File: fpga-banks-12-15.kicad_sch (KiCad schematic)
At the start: 17 parts, among them U15 XC7K160T-FFG676

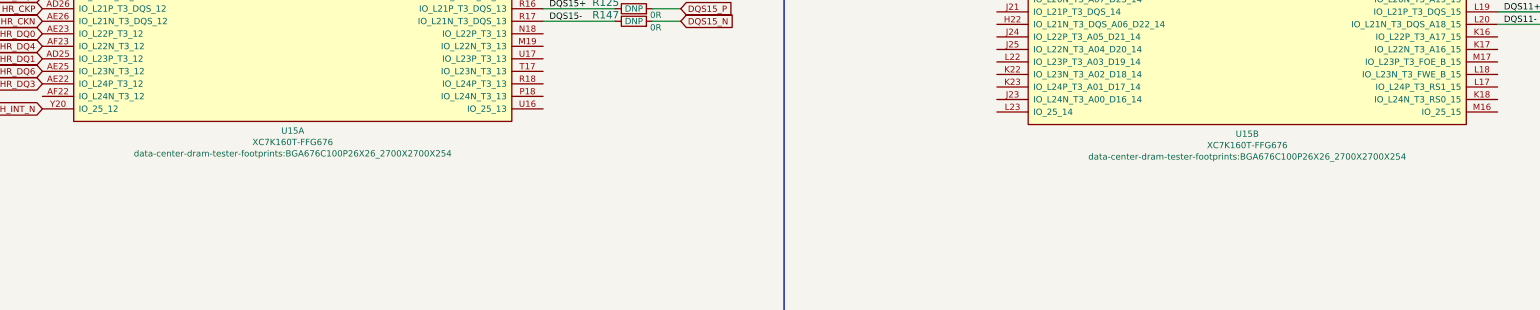
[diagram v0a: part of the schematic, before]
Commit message: Update FPGA symbol (die to pad length), initial fanout for die [1..4]
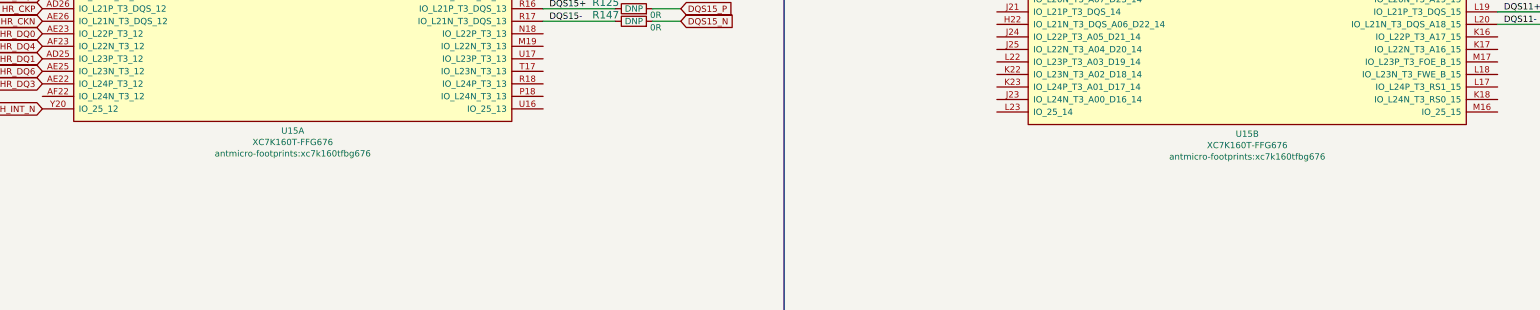
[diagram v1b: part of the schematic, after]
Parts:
- U15: footprint data-center-dram-tester-footprints:BGA676C100P26X26_2700X2700X254 -> antmicro-footprints:xc7k160tfbg676
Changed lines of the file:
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@@
     (property "Reference" "U15" (id 0) (at 110.49 220.98 0))
     (property "Value" "XC7K160T-FFG676" (id 1) (at 110.49 223.2914 0))
-    (property "Footprint" "data-center-dram-tester-footprints:BGA676C100P26X26_2700X2700X254" (id 2) (at 110.49 225.6028 0))
+    (property "Footprint" "antmicro-footprints:xc7k160tfbg676" (id 2) (at 110.49 225.6028 0))
     (property "Datasheet" "" (id 3) (at 110.49 145.415 0))
     (pin "AA21")
@@
     (property "Reference" "U15" (id 0) (at 304.165 221.615 0))
     (property "Value" "XC7K160T-FFG676" (id 1) (at 304.165 223.9264 0))
-    (property "Footprint" "data-center-dram-tester-footprints:BGA676C100P26X26_2700X2700X254" (id 2) (at 304.165 226.2378 0))
+    (property "Footprint" "antmicro-footprints:xc7k160tfbg676" (id 2) (at 304.165 226.2378 0))
     (property "Datasheet" "" (id 3) (at 304.165 146.05 0))
     (pin "AA21")

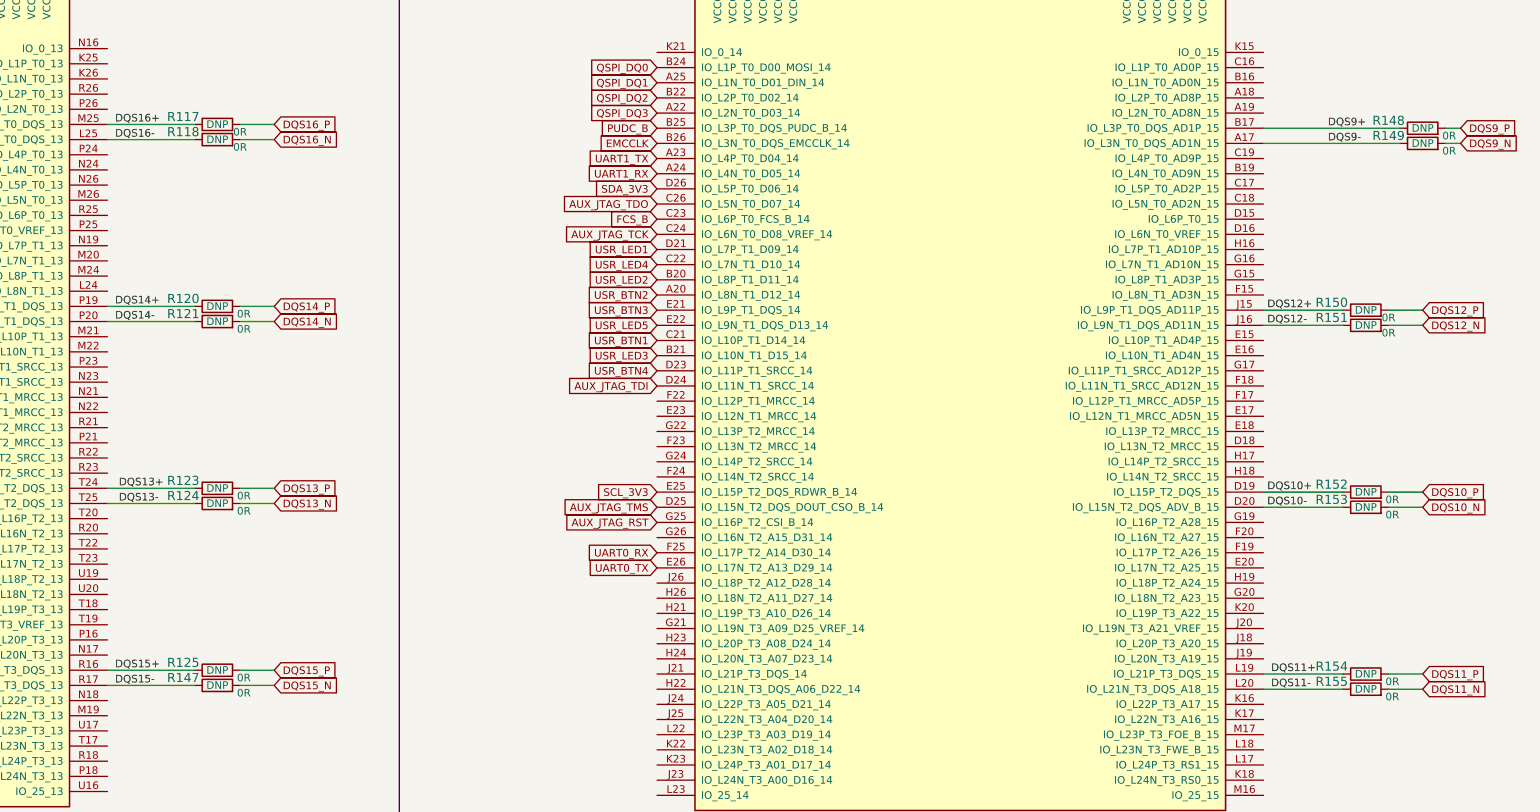
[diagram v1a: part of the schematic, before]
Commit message: Add new pinout for bank 32 and 34, create custom DRC rules for DDR, initial routing for die 6,7,9
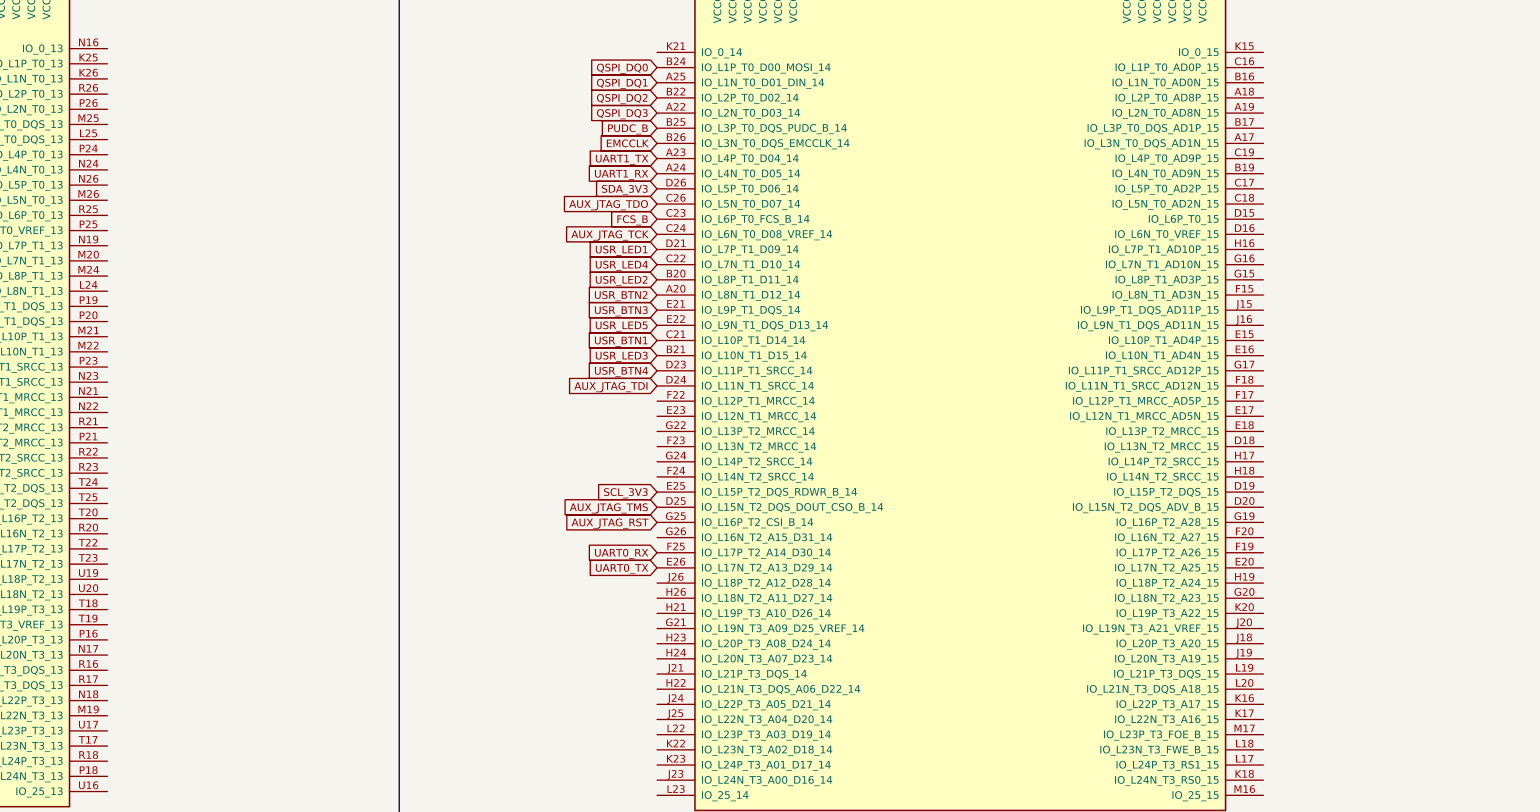
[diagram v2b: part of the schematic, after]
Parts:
- removed R117, R118, R120, R121, R123, R124, R125, R147, R148, R149, R150, R151, R152, R153, R154, R155: R_0R_0201, data-center-dram-tester-footprints:0201-res, symbol data-center-dram-tester:R_0R_0201
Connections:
- net DQS10+: no longer names the net of U15.D19 (IO_L15P_T2_DQS_15)
- net DQS10-: no longer names the net of U15.D20 (IO_L15N_T2_DQS_ADV_B_15)
- net DQS11+: no longer names the net of U15.L19 (IO_L21P_T3_DQS_15)
- net DQS11-: no longer names the net of U15.L20 (IO_L21N_T3_DQS_A18_15)
- net DQS12+: no longer names the net of U15.J15 (IO_L9P_T1_DQS_AD11P_15)
- net DQS12-: no longer names the net of U15.J16 (IO_L9N_T1_DQS_AD11N_15)
- net DQS13+: no longer names the net of U15.T24 (IO_L15P_T2_DQS_13)
- net DQS13-: no longer names the net of U15.T25 (IO_L15N_T2_DQS_13)
- net DQS14+: no longer names the net of U15.P19 (IO_L9P_T1_DQS_13)
- net DQS14-: no longer names the net of U15.P20 (IO_L9N_T1_DQS_13)
- net DQS15+: no longer names the net of U15.R16 (IO_L21P_T3_DQS_13)
- net DQS15-: no longer names the net of U15.R17 (IO_L21N_T3_DQS_13)
- net DQS16+: no longer names the net of U15.M25 (IO_L3P_T0_DQS_13)
- net DQS16-: no longer names the net of U15.L25 (IO_L3N_T0_DQS_13)
- net DQS9+: no longer names the net of U15.B17 (IO_L3P_T0_DQS_AD1P_15)
- net DQS9-: no longer names the net of U15.A17 (IO_L3N_T0_DQS_AD1N_15)

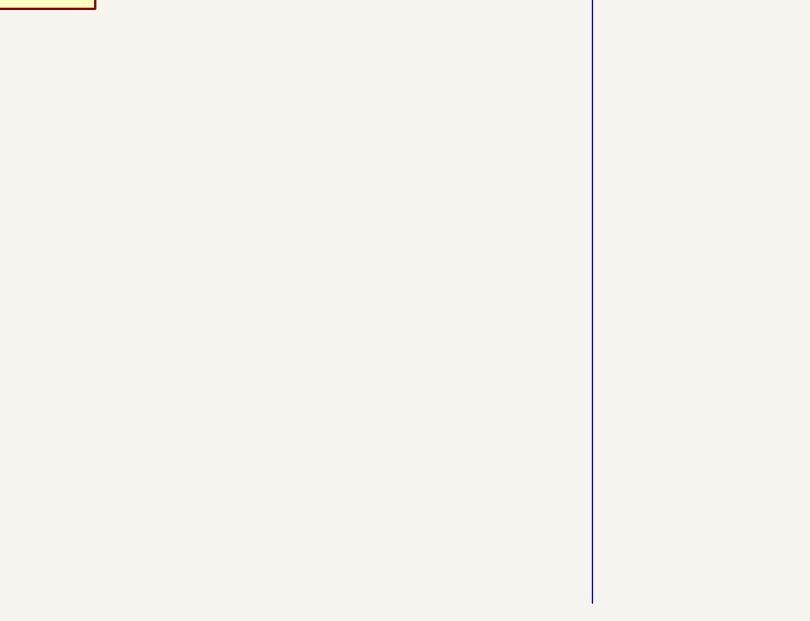
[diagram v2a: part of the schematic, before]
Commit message: Finish assigning address, command and control pins. Finish initial rerouting of DDR4 interface
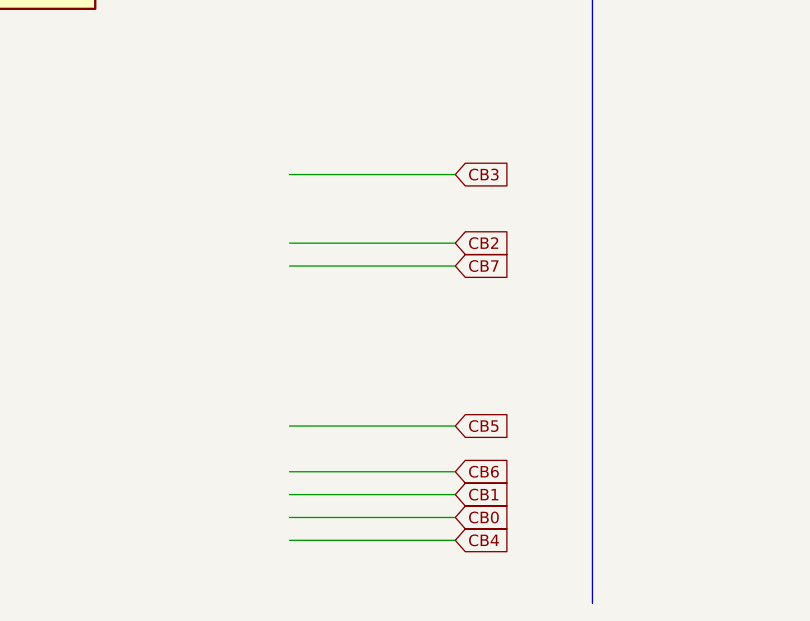
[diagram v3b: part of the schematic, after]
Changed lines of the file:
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@@
+    (stroke (width 0) (type default) (color 0 0 0 0))
+  )
+  (wire (pts (xy 176.53 278.13) (xy 194.945 278.13))
     (stroke (width 0) (type default) (color 0 0 0 0))
   )
@@
     (stroke (width 0) (type default) (color 0 0 0 0))
   )
+  (wire (pts (xy 176.53 270.51) (xy 194.945 270.51))
+    (stroke (width 0) (type default) (color 0 0 0 0))
+  )
   (wire (pts (xy 140.97 66.04) (xy 143.51 66.04))
     (stroke (width 0) (type default) (color 0 0 0 0))
@@
     (stroke (width 0) (type default) (color 0 0 0 0))
   )
+  (wire (pts (xy 176.53 275.59) (xy 194.945 275.59))
+    (stroke (width 0) (type default) (color 0 0 0 0))
+  )
   (wire (pts (xy 74.93 71.755) (xy 74.93 66.04))
     (stroke (width 0) (type default) (color 0 0 0 0))
@@
     (stroke (width 0) (type default) (color 0 0 0 0))
   )
+  (wire (pts (xy 176.53 265.43) (xy 194.945 265.43))
+    (stroke (width 0) (type default) (color 0 0 0 0))
+  )
   (wire (pts (xy 151.13 71.755) (xy 151.13 66.04))
     (stroke (width 0) (type default) (color 0 0 0 0))
@@
     (stroke (width 0) (type default) (color 0 0 0 0))
   )
+  (wire (pts (xy 176.53 247.65) (xy 194.945 247.65))
+    (stroke (width 0) (type default) (color 0 0 0 0))
+  )
   (wire (pts (xy 88.9 66.04) (xy 88.9 62.23))
     (stroke (width 0) (type default) (color 0 0 0 0))
@@
     (stroke (width 0) (type default) (color 0 0 0 0))
   )
+  (wire (pts (xy 176.53 237.49) (xy 194.945 237.49))
+    (stroke (width 0) (type default) (color 0 0 0 0))
+  )
   (wire (pts (xy 72.39 66.04) (xy 74.93 66.04))
     (stroke (width 0) (type default) (color 0 0 0 0))
@@
     (stroke (width 0) (type default) (color 0 0 0 0))
   )
+  (wire (pts (xy 176.53 245.11) (xy 194.945 245.11))
+    (stroke (width 0) (type default) (color 0 0 0 0))
+  )
   (wire (pts (xy 266.065 72.39) (xy 266.065 66.675))
+    (stroke (width 0) (type default) (color 0 0 0 0))
+  )
+  (wire (pts (xy 176.53 273.05) (xy 194.945 273.05))
     (stroke (width 0) (type default) (color 0 0 0 0))
   )
@@
     )
   )
+  (global_label "CB6" (shape input) (at 194.945 270.51 0) (fields_autoplaced)
+    (effects (font (size 1.27 1.27)) (justify left))
+    (property "Intersheet References" "${INTERSHEET_REFS}" (id 0) (at -177.165 76.835 0)
+      (effects (font (size 1.27 1.27)) hide)
+    )
+  )
   (global_label "HR_CKP" (shape input) (at 59.69 196.215 180) (fields_autoplaced)
     (effects (font (size 1.27 1.27)) (justify right))
@@
     )
   )
+  (global_label "CB5" (shape input) (at 194.945 265.43 0) (fields_autoplaced)
+    (effects (font (size 1.27 1.27)) (justify left))
+    (property "Intersheet References" "${INTERSHEET_REFS}" (id 0) (at -177.165 76.835 0)
+      (effects (font (size 1.27 1.27)) hide)
+    )
+  )
   (global_label "HR_DQ6" (shape input) (at 59.69 208.915 180) (fields_autoplaced)
     (effects (font (size 1.27 1.27)) (justify right))
@@
     )
   )
+  (global_label "CB0" (shape input) (at 194.945 275.59 0) (fields_autoplaced)
+    (effects (font (size 1.27 1.27)) (justify left))
+    (property "Intersheet References" "${INTERSHEET_REFS}" (id 0) (at -177.165 76.835 0)
+      (effects (font (size 1.27 1.27)) hide)
+    )
+  )
   (global_label "AUX_JTAG_TDI" (shape input) (at 253.365 148.59 180) (fields_autoplaced)
     (effects (font (size 1.27 1.27)) (justify right))
@@
     (effects (font (size 1.27 1.27)) (justify right))
     (property "Intersheet References" "${INTERSHEET_REFS}" (id 0) (at 0 0 0)
+      (effects (font (size 1.27 1.27)) hide)
+    )
+  )
+  (global_label "CB7" (shape input) (at 194.945 247.65 0) (fields_autoplaced)
+    (effects (font (size 1.27 1.27)) (justify left))
+    (property "Intersheet References" "${INTERSHEET_REFS}" (id 0) (at -177.165 76.835 0)
       (effects (font (size 1.27 1.27)) hide)
     )
@@
     )
   )
+  (global_label "CB4" (shape input) (at 194.945 278.13 0) (fields_autoplaced)
+    (effects (font (size 1.27 1.27)) (justify left))
+    (property "Intersheet References" "${INTERSHEET_REFS}" (id 0) (at -177.165 76.835 0)
+      (effects (font (size 1.27 1.27)) hide)
+    )
+  )
+  (global_label "CB2" (shape input) (at 194.945 245.11 0) (fields_autoplaced)
+    (effects (font (size 1.27 1.27)) (justify left))
+    (property "Intersheet References" "${INTERSHEET_REFS}" (id 0) (at -177.165 76.835 0)
+      (effects (font (size 1.27 1.27)) hide)
+    )
+  )
   (global_label "ETH_REF_CLK" (shape input) (at 59.69 145.415 180) (fields_autoplaced)
     (effects (font (size 1.27 1.27)) (justify right))
@@
     )
   )
+  (global_label "CB1" (shape input) (at 194.945 273.05 0) (fields_autoplaced)
+    (effects (font (size 1.27 1.27)) (justify left))
+    (property "Intersheet References" "${INTERSHEET_REFS}" (id 0) (at -177.165 76.835 0)
+      (effects (font (size 1.27 1.27)) hide)
+    )
+  )
   (global_label "ETH_TXD1" (shape input) (at 59.69 142.875 180) (fields_autoplaced)
     (effects (font (size 1.27 1.27)) (justify right))
@@
       (effects (font (size 1.27 1.27)) hide)
     )
+  )
+  (global_label "CB3" (shape input) (at 194.945 237.49 0) (fields_autoplaced)
+    (effects (font (size 1.27 1.27)) (justify left))
+    (property "Intersheet References" "${INTERSHEET_REFS}" (id 0) (at -177.165 76.835 0)
+      (effects (font (size 1.27 1.27)) hide)
+    )
